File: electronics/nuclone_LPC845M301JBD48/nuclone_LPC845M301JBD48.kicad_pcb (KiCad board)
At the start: 2 copper layers, 48.3 x 76.2 mm, 53 parts, among them J1 JTAG_2X05, J2 USB-ID, J3 nuclone_small_left, J4 nuclone_small_right, SW1 RESET, U1 MCP1702-MB, U2 LPC1125FBD48_303, Y1 12MHz

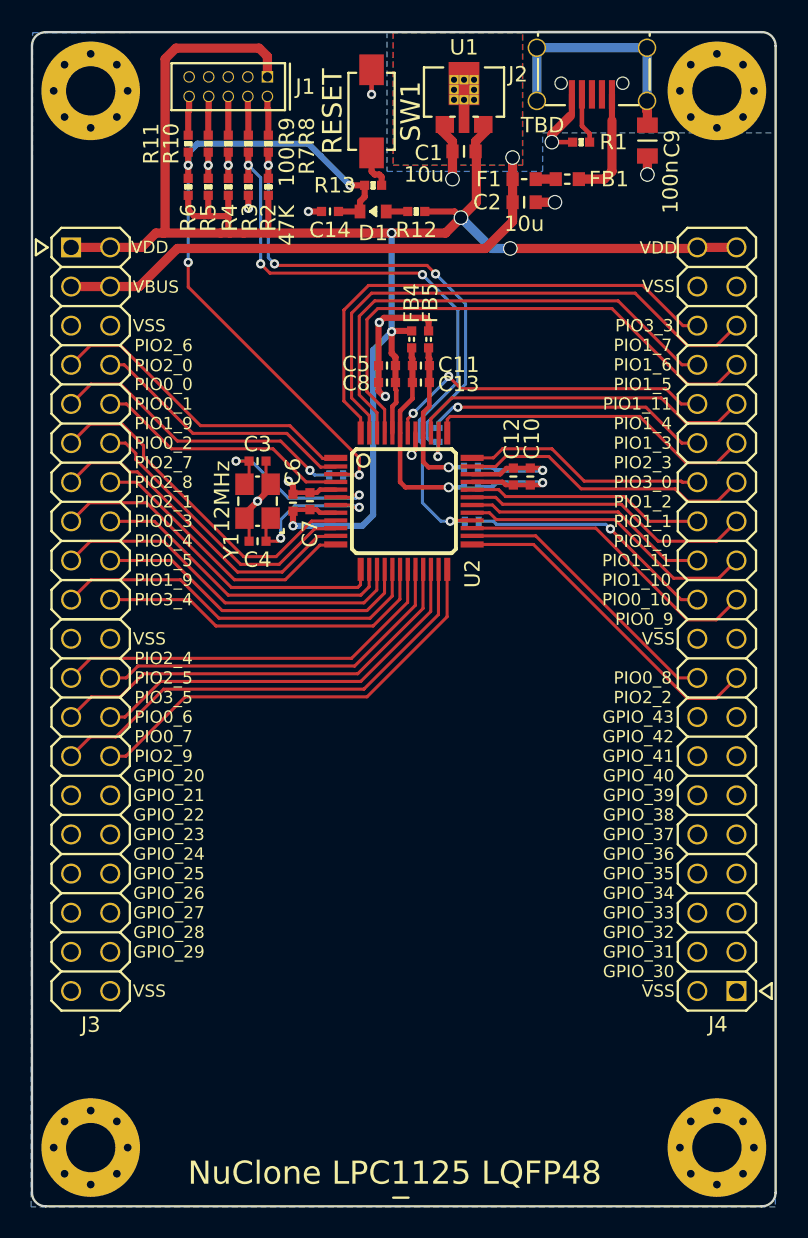
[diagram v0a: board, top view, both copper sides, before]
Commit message: minor fixes in schematic, initial placement of all components, all ERC checks pass
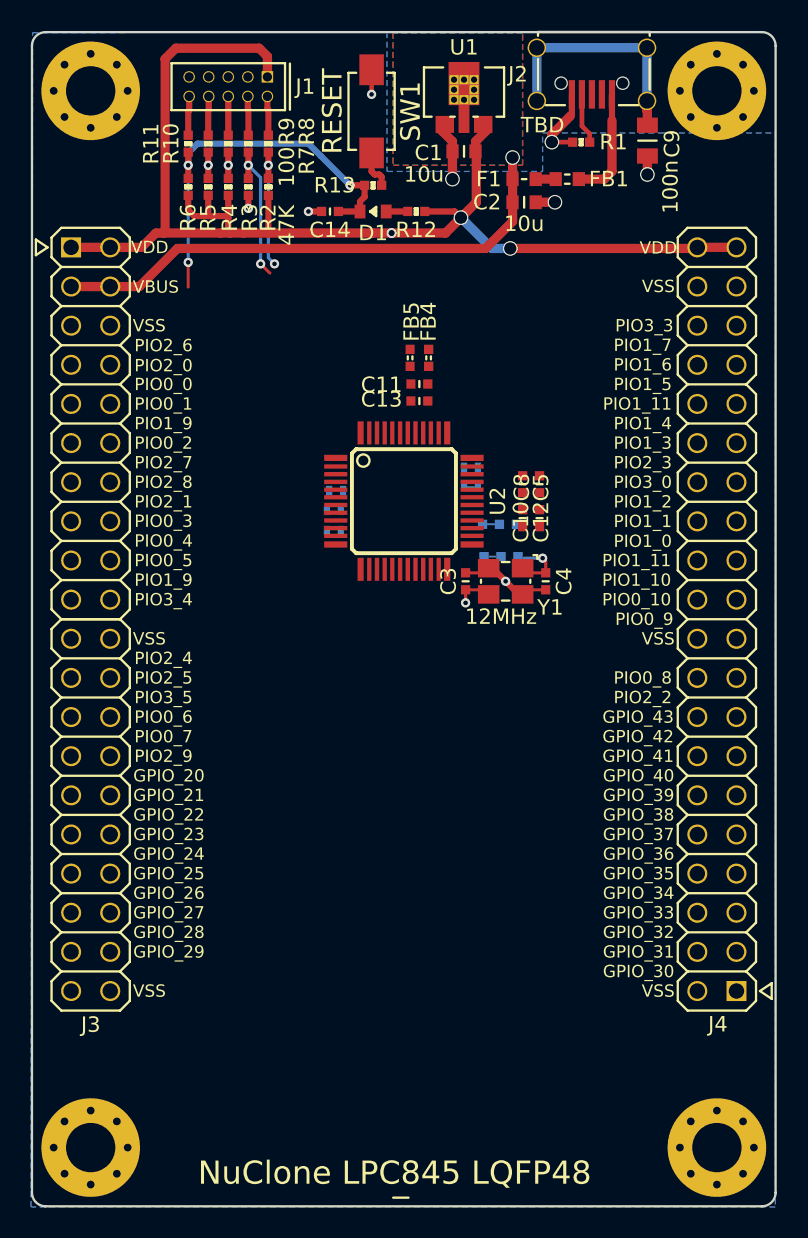
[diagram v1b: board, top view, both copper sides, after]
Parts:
- removed C6: 1u, SquantorRcl:C_0402
- removed C7: 100n, SquantorRcl:C_0402
- added JP6: PIO_8/XTAL, SquantorSpecial:solder_jumper_3way_12conn, B.Cu at (91.3, 92.9)
- added JP7: PIO_9/XTAL, SquantorSpecial:solder_jumper_3way_12conn, B.Cu at (91.4, 95.0)
- N2: value 20201205 -> 20201206
- N4: value NuClone LPC1125 LQFP48 -> NuClone LPC845 LQFP48
- U2: value LPC1125FBD48_303 -> LPC845M301JBD48
- moved C4 18.9 mm to (94.3, 96.6), turned to 270 degrees
- moved Y1 16.9 mm to (91.7, 96.6), turned to 180 degrees
- moved C3 15.6 mm to (89.1, 96.6), turned to 90 degrees
- moved C5 14.0 mm to (93.9, 92.5), turned to 90 degrees
- moved C8 12.4 mm to (92.8, 92.5), turned to 90 degrees
- moved JP3 9.17 mm to (80.5, 93.3), turned to 0 degrees
- moved JP2 8.98 mm to (80.5, 92.0), turned to 0 degrees
- moved C12 1.77 mm to (93.9, 90.3), turned to 270 degrees
- moved FB5 1.70 mm to (85.5, 82.1)
- moved FB4 1.63 mm to (86.7, 82.1)
- moved C11 1.20 mm to (86.1, 83.8), turned to 180 degrees
- moved C13 1.20 mm to (86.1, 84.9), turned to 180 degrees
- moved JP1 1.00 mm to (80.7, 90.7)
- moved C10 0.71 mm to (92.8, 90.3), turned to 270 degrees
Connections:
- net /PIO2_0 renamed /PIO0_13
- net /PIO3_3 renamed /PIO0_17
- C3 pad 1: Net-(C3-Pad1) -> /XTALOUT
- C4 pad 1: Net-(C4-Pad1) -> /XTALIN
- J3 pad 10: /PIO0_1 -> /PIO0_12
- J3 pad 11: /PIO1_8 -> /PIO0_5
- J3 pad 12: /PIO0_2 -> /PIO0_4
- J3 pad 13: /PIO2_7 -> /PIO0_28
- J3 pad 14: /PIO2_8 -> /PIO0_3
- J3 pad 15: /PIO2_1 -> /PIO0_31
- J3 pad 16: /PIO0_3 -> /PIO0_2
- J3 pad 17: /PIO0_4 -> /PIO1_0
- J3 pad 18: /PIO0_5 -> /PIO0_11
- J3 pad 19: /PIO1_9 -> /PIO0_10
- J3 pad 20: /PIO3_4 -> /PIO1_1
- J3 pad 23: /PIO2_4 -> /PIO0_16
- J3 pad 24: /PIO2_5 -> /PIO1_2
- J3 pad 25: /PIO3_5 -> /PIO0_27
- J3 pad 26: /PIO0_6 -> /PIO0_26
- J3 pad 27: /PIO0_7 -> /PIO0_25
- J3 pad 28: /PIO2_9 -> /PIO0_24
- J3 pad 29: /GPIO_20 -> /PIO1_3
- J3 pad 30: /GPIO_21 -> /PIO0_15
- J3 pad 31: /GPIO_22 -> /PIO1_4
- J3 pad 32: /GPIO_23 -> /PIO0_1
- J3 pad 7: /PIO2_6 -> /PIO1_8
- J3 pad 9: /PIO0_0 -> /PIO1_9
- J4 pad 17: /PIO2_2 -> /PIO0_9
- J4 pad 21: /PIO0_9 -> /PIO1_5
- J4 pad 22: /PIO0_10 -> /PIO1_6
- J4 pad 23: /PIO1_10 -> /PIO0_7
- J4 pad 24: /PIO0_11 -> /PIO0_6
- J4 pad 25: /PIO1_0 -> /PIO1_7
- J4 pad 26: /PIO1_1 -> /PIO0_0
- J4 pad 27: /PIO1_2 -> /PIO0_14
- J4 pad 28: /PIO3_0 -> /PIO0_29
- J4 pad 29: /PIO2_3 -> /PIO0_23
- J4 pad 30: /PIO1_3 -> /PIO0_30
- J4 pad 31: /PIO1_4 -> /PIO0_22
- J4 pad 32: /PIO1_11 -> /PIO0_21
- J4 pad 33: /PIO1_5 -> /PIO0_20
- J4 pad 34: /PIO1_6 -> /PIO0_19
- J4 pad 35: /PIO1_7 -> /PIO0_18
- JP1 pad 1: /PIO0_0 -> /PIO0_5
- JP2 pad 1: /PIO0_10 -> /PIO0_3
- JP3 pad 1: /PIO1_3 -> /PIO0_2
- U2 pad 1: /PIO2_6 -> /PIO1_8
- U2 pad 10: /PIO0_2 -> /TMS
- U2 pad 11: /PIO2_7 -> /PIO1_0
- U2 pad 12: /PIO2_8 -> /PIO0_11
- U2 pad 13: /PIO2_1 -> /PIO0_10
- U2 pad 14: /PIO0_3 -> /PIO1_1
- U2 pad 15: /PIO0_4 -> /PIO0_16
- U2 pad 16: /PIO0_5 -> /PIO1_2
- U2 pad 17: /PIO1_9 -> /PIO0_27
- U2 pad 18: /PIO3_4 -> /PIO0_26
- U2 pad 19: /PIO2_4 -> /PIO0_25
- U2 pad 20: /PIO2_5 -> /PIO0_24
- U2 pad 21: /PIO3_5 -> /PIO1_3
- U2 pad 22: /PIO0_6 -> /PIO0_15
- U2 pad 23: /PIO0_7 -> /PIO1_4
- U2 pad 24: /PIO2_9 -> /PIO0_1
- U2 pad 25: /PIO2_2 -> /PIO0_9_I
- U2 pad 26: /PIO0_8 -> /PIO0_8_I
- U2 pad 27: /PIO0_9 -> /PIO1_5
- U2 pad 28: /TCK -> /PIO1_6
- U2 pad 29: /PIO1_10 -> /VDD
- U2 pad 3: /RESET -> /PIO1_9
- U2 pad 30: /PIO0_11 -> /VSS
- U2 pad 31: /PIO1_0 -> /VREFN
- U2 pad 32: /PIO1_1 -> /VREFP
- U2 pad 33: /VREFP -> /PIO0_7
- U2 pad 34: /VREFN -> /PIO0_6
- U2 pad 35: /PIO1_2 -> /PIO1_7
- U2 pad 36: /PIO3_0 -> /PIO0_0
- U2 pad 37: /PIO2_3 -> /PIO0_14
- U2 pad 38: /TMS -> /PIO0_29
- U2 pad 39: /PIO1_4 -> /PIO0_23
- U2 pad 4: /PIO0_1 -> /PIO0_12
- U2 pad 40: /VSSA -> /VDDA
- U2 pad 41: /VSS -> /VSSA
- U2 pad 42: /PIO1_11 -> /PIO0_30
- U2 pad 43: /VDDA -> /PIO0_22
- U2 pad 44: /VDD -> /PIO0_21
- U2 pad 45: /PIO1_5 -> /PIO0_20
- U2 pad 46: /PIO1_6 -> /PIO0_19
- U2 pad 47: /PIO1_7 -> /PIO0_18
- U2 pad 5: /VSS -> /RESET
- U2 pad 6: Net-(C3-Pad1) -> /PIO0_4
- U2 pad 7: Net-(C4-Pad1) -> /PIO0_28
- U2 pad 8: /VDD -> /TCK
- U2 pad 9: /PIO1_8 -> /PIO0_31
- Y1 pad 1: Net-(C4-Pad1) -> /XTALIN
- Y1 pad 3: Net-(C3-Pad1) -> /XTALOUT
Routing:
- net /VDD: track 120.5 -> 84.2 mm, vias 5 -> 3
- net /PIO1_7: track 35.7 -> 0.00 mm
- net /PIO1_5: track 34.7 -> 0.00 mm
- net /PIO0_17: track 33.1 -> 0.00 mm
- net /PIO1_6: track 32.1 -> 0.00 mm
- net /TCK: track 40.8 -> 9.28 mm, vias 4 -> 2
- net /PIO0_7: track 30.5 -> 0.00 mm
- net /PIO2_9: track 28.6 -> 0.00 mm
- net /PIO3_5: track 28.3 -> 0.00 mm
- net /TMS: track 34.8 -> 8.41 mm, vias 4 -> 2
- net /PIO0_6: track 26.3 -> 0.00 mm
- net /PIO2_4: track 26.0 -> 0.00 mm
- net /PIO1_9: track 24.7 -> 0.00 mm
- net /PIO2_5: track 24.0 -> 0.00 mm
- net /PIO0_4: track 23.7 -> 0.00 mm
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
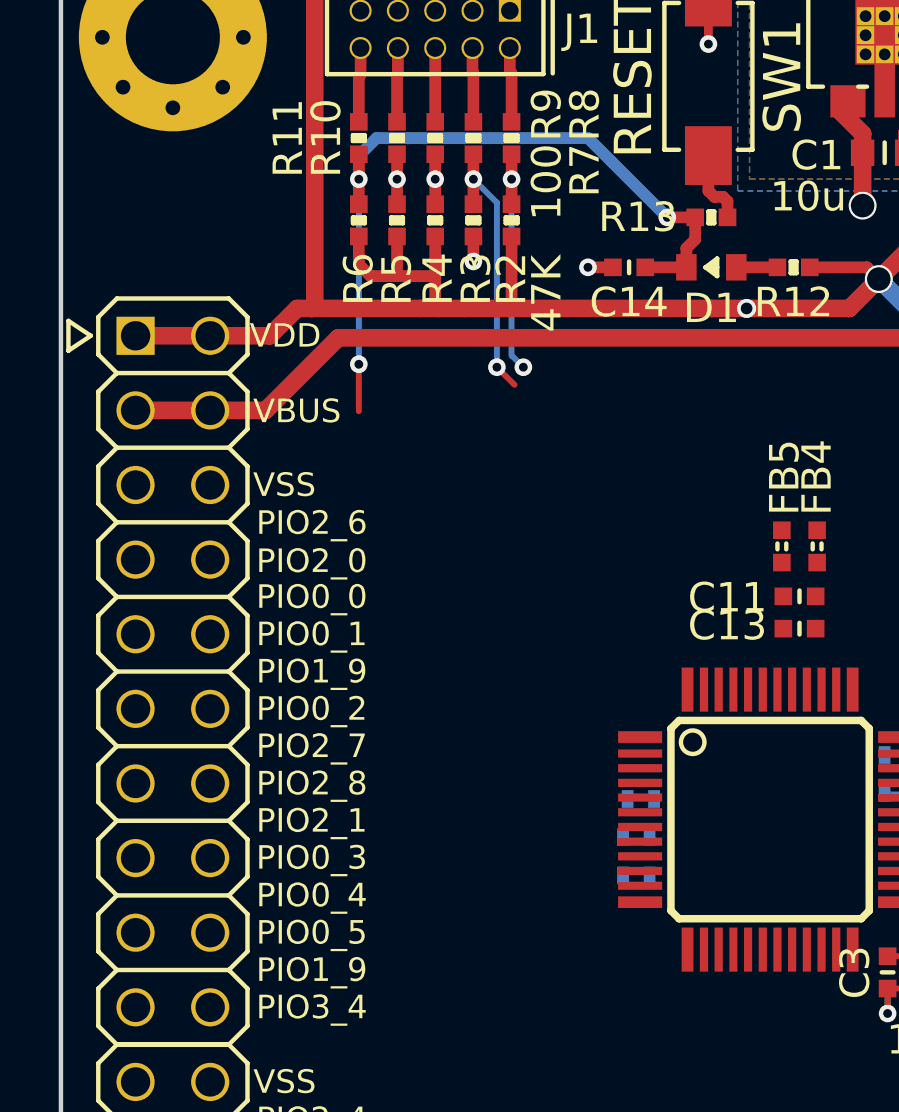
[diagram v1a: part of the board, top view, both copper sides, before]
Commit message: routed SWD bus, and first side of GPIO's
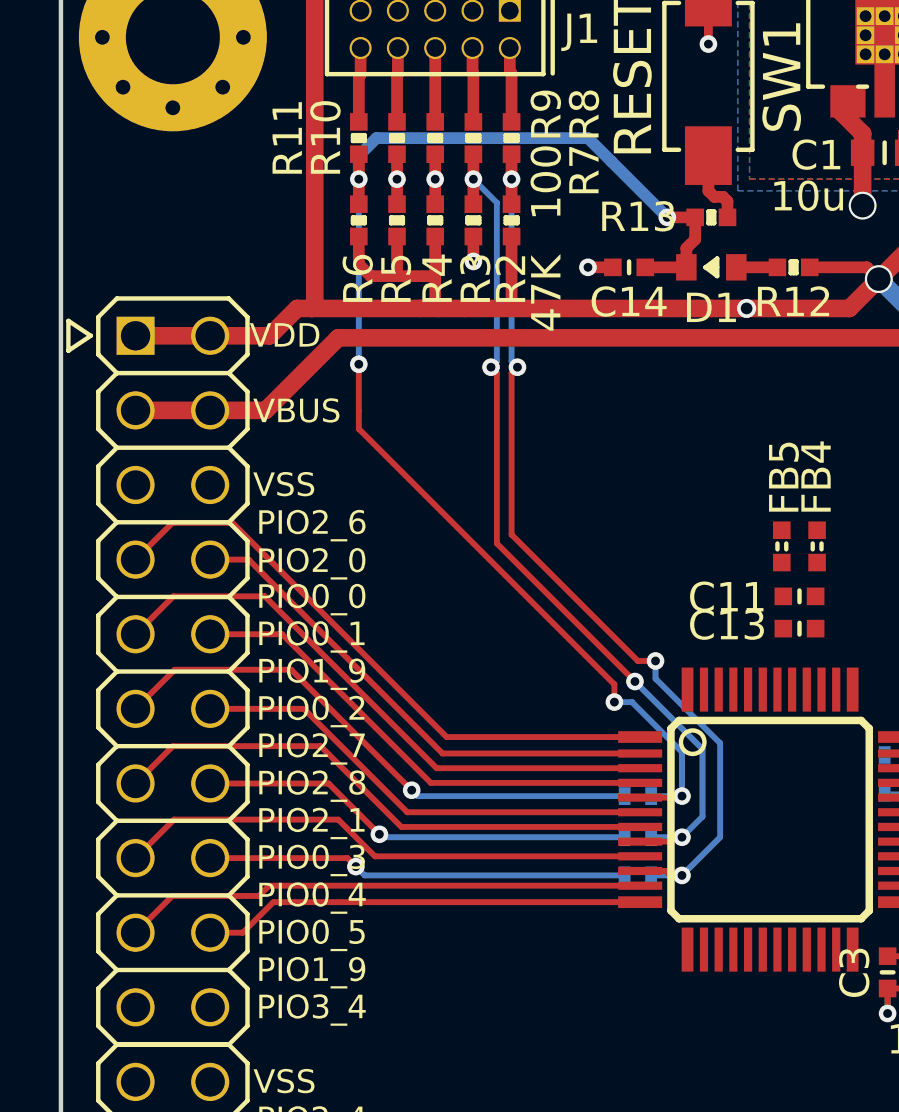
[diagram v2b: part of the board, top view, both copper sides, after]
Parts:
- moved JP1 0.14 mm to (80.6, 90.6)
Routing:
- net /TMS: track 8.41 -> 31.9 mm, vias 2 -> 4
- net /TCK: track 9.28 -> 30.3 mm, vias 2 -> 4
- net /PIO1_8: track 0.00 -> 20.7 mm
- net /RESET: track 26.4 -> 46.9 mm, vias 3 -> 5
- net /PIO1_9: track 0.00 -> 20.1 mm
- net /PIO0_5: track 0.00 -> 19.0 mm, vias 0 -> 1
- net /PIO0_28: track 0.00 -> 18.8 mm
- net /PIO0_31: track 0.00 -> 18.2 mm
- net /PIO1_0: track 0.00 -> 17.8 mm
- net /PIO0_13: track 0.00 -> 17.4 mm
- net /PIO0_12: track 0.00 -> 16.7 mm
- net /PIO0_4: track 0.00 -> 16.1 mm
- net /PIO0_11: track 0.00 -> 15.1 mm
- net /PIO0_3: track 0.00 -> 14.9 mm, vias 0 -> 1
- net /PIO0_2: track 0.00 -> 14.4 mm, vias 0 -> 1

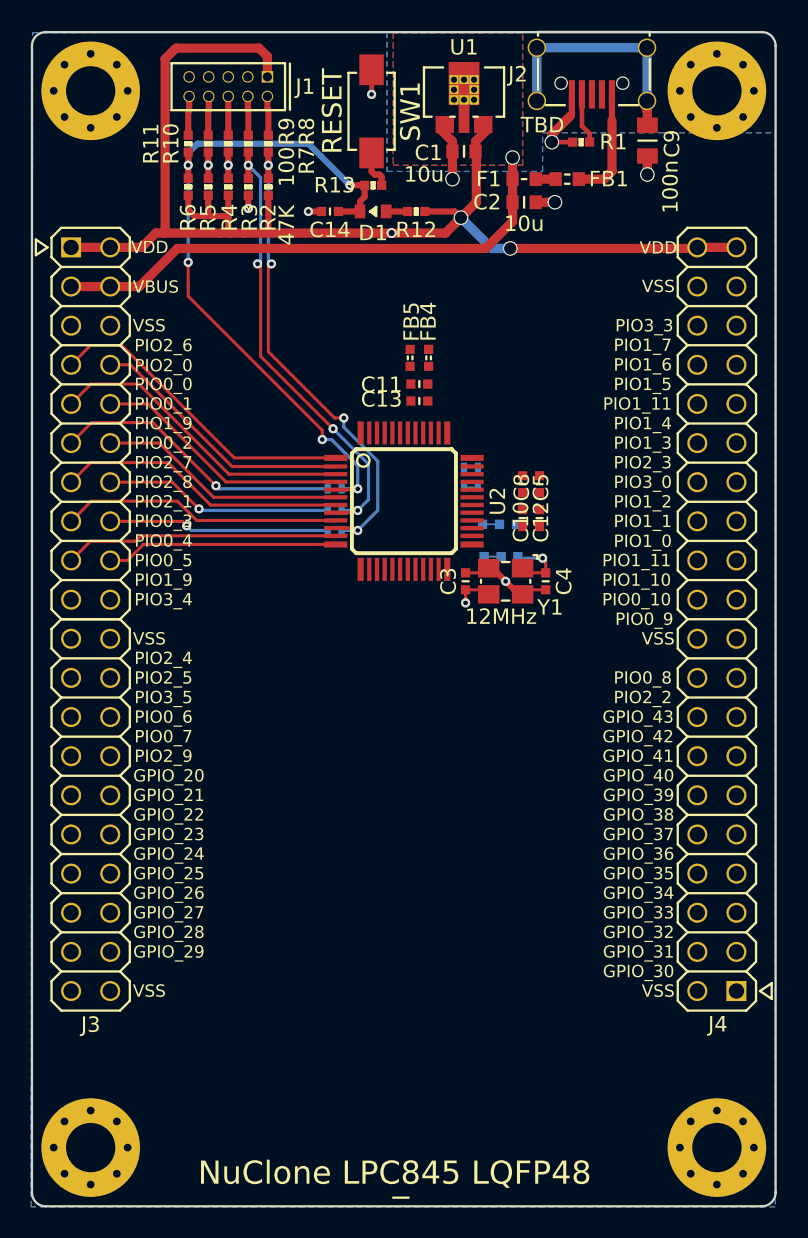
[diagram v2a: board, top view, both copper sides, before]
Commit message: routed additional side, and crystal
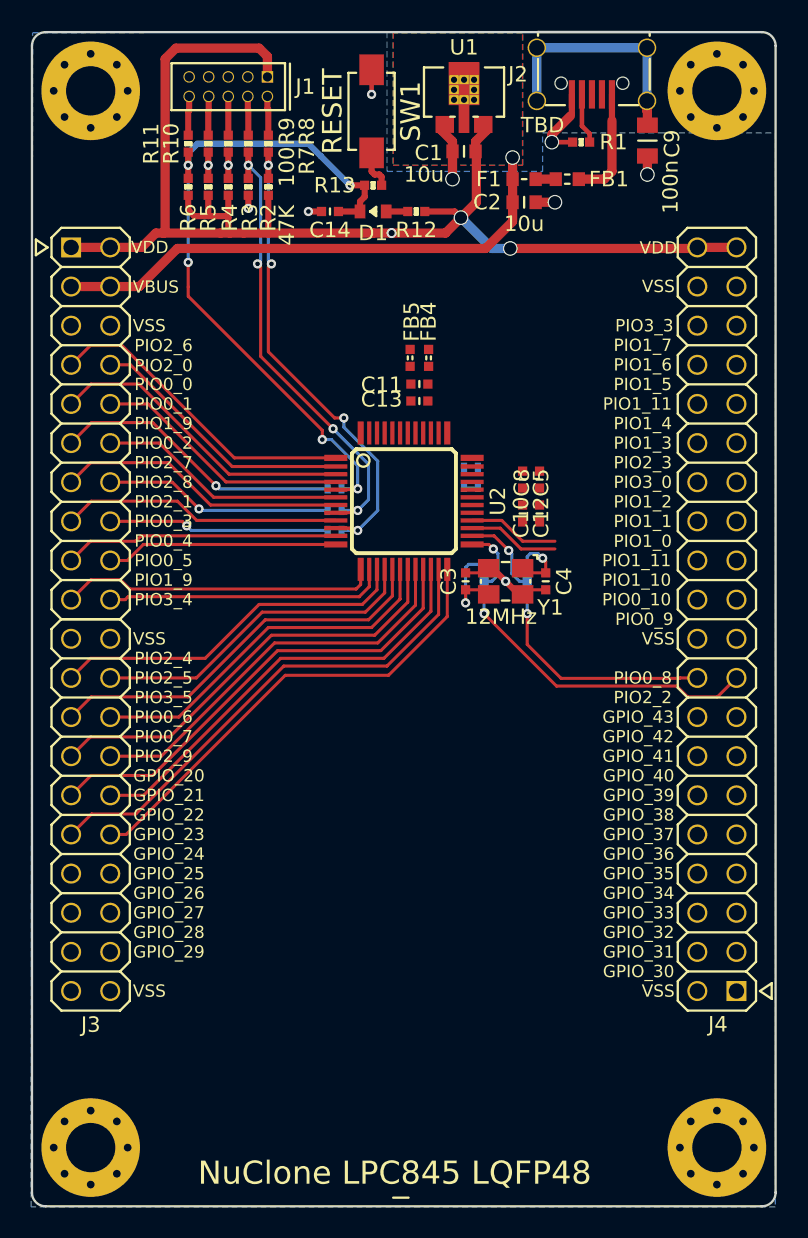
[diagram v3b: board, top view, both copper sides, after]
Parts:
- moved JP6 4.11 mm to (93.1, 96.6), turned to 270 degrees
- moved JP7 1.94 mm to (90.3, 96.6), turned to 270 degrees
- moved C10 0.30 mm to (92.8, 90.0)
- moved C12 0.30 mm to (93.9, 90.0)
- moved C5 0.30 mm to (93.9, 92.2)
- moved C8 0.30 mm to (92.8, 92.2)
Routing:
- net /PIO1_4: track 0.00 -> 32.7 mm
- net /PIO0_1: track 0.00 -> 30.8 mm
- net /PIO1_3: track 0.00 -> 30.4 mm
- net /PIO0_15: track 0.00 -> 28.5 mm
- net /PIO0_25: track 0.00 -> 28.1 mm
- net /PIO0_24: track 0.00 -> 26.2 mm
- net /PIO0_27: track 0.00 -> 25.8 mm
- net /PIO0_26: track 0.00 -> 23.9 mm
- net /PIO0_16: track 0.00 -> 23.5 mm
- net /PIO1_2: track 0.00 -> 21.6 mm
- net /PIO0_10: track 0.00 -> 20.7 mm
- net /PIO0_9: track 0.00 -> 20.1 mm, vias 0 -> 1
- net /PIO1_1: track 0.00 -> 18.3 mm
- net /PIO0_8: track 0.00 -> 15.0 mm, vias 0 -> 1
- net /PIO1_6: track 0.00 -> 5.93 mm
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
